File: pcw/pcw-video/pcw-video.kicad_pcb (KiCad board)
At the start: 2 copper layers, 15 parts, among them J1 video in, J2 keyboard in, J3 video out, J4 composite out, J5 video config, J7 keyboard out, U1 74HC00

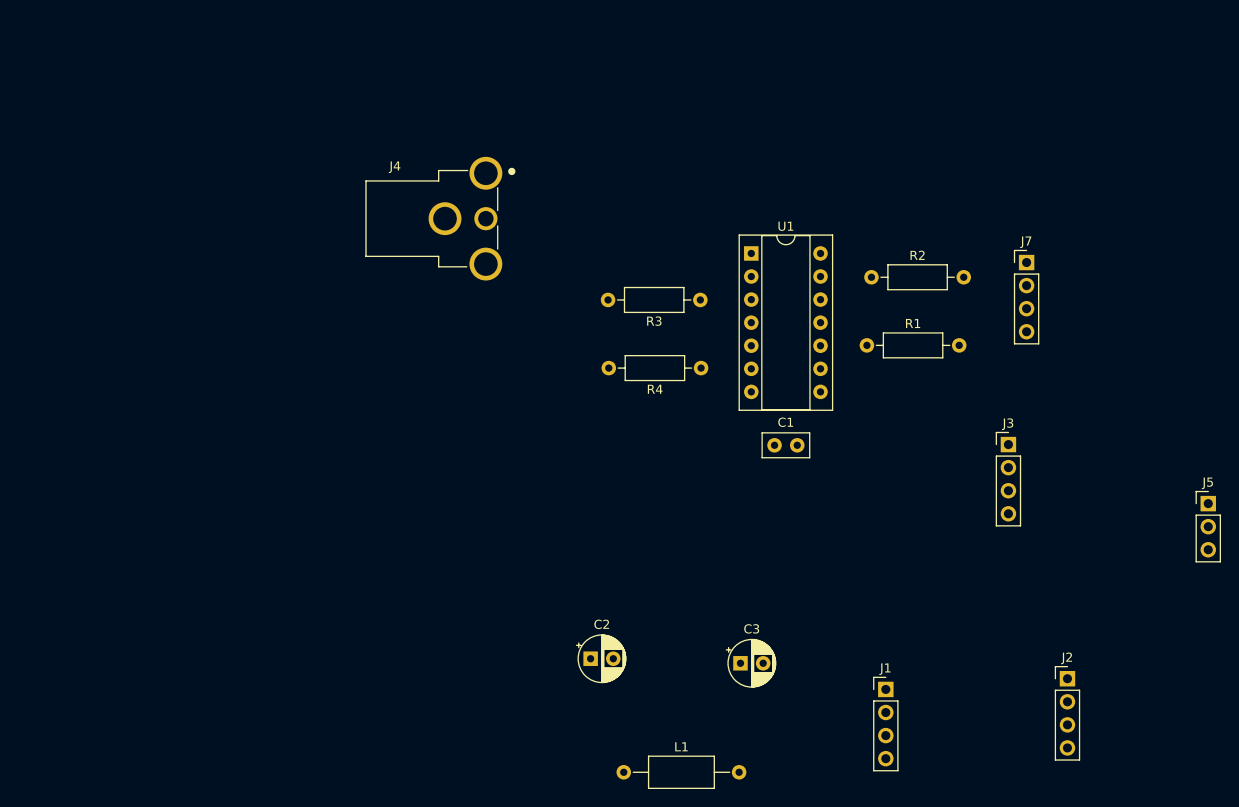
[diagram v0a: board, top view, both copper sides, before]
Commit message: [pcw] initial component placement
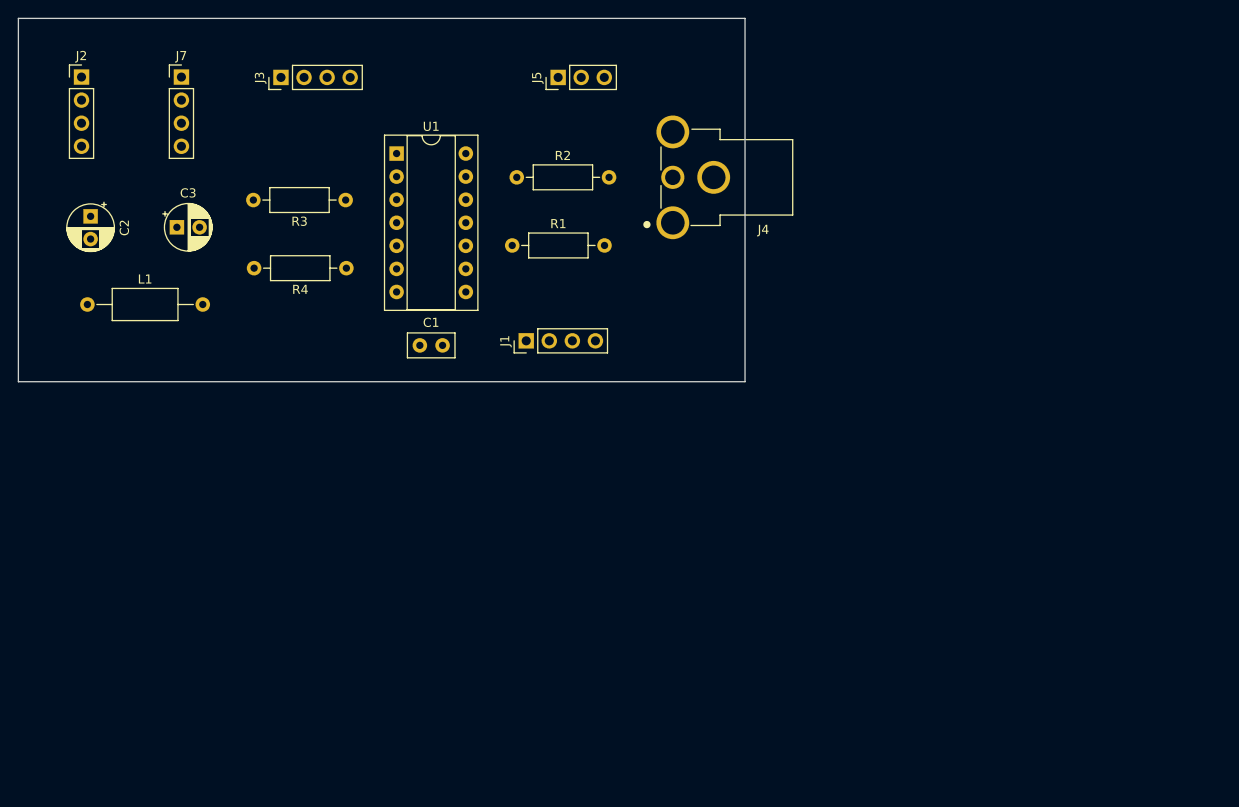
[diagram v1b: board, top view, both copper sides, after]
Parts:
- moved J2 127.2 mm to (21.9, 21.0)
- moved J7 95.3 mm to (33.0, 21.0)
- moved J3 89.7 mm to (43.9, 21.0), turned to 90 degrees
- moved J5 85.6 mm to (74.4, 21.0), turned to 90 degrees
- moved C3 78.4 mm to (32.5, 37.5)
- moved L1 78.4 mm to (22.6, 46.0)
- moved C2 73.5 mm to (22.9, 36.3), turned to -90 degrees
- moved J1 55.1 mm to (70.9, 50.0), turned to 90 degrees
- moved C1 40.6 mm to (59.2, 50.5)
- moved R1 40.6 mm to (69.4, 39.5)
- moved R2 40.6 mm to (69.9, 32.0)
- moved R3 40.6 mm to (51.0, 34.5)
- moved R4 40.6 mm to (51.1, 42.0)
- moved U1 40.6 mm to (56.6, 29.4)
- moved J4 32.8 mm to (93.0, 32.0), turned to 180 degrees
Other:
- board outline added: 80 x 40 mm
